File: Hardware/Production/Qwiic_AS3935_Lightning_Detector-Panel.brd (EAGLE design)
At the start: 123.2 x 123.2 mm, 1075 parts, among them U1 AS3935, U10 AS3935, U11 AS3935, U12 AS3935, U13 AS3935, U14 AS3935, U15 AS3935, U16 AS3935, U2 AS3935, U3 AS3935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

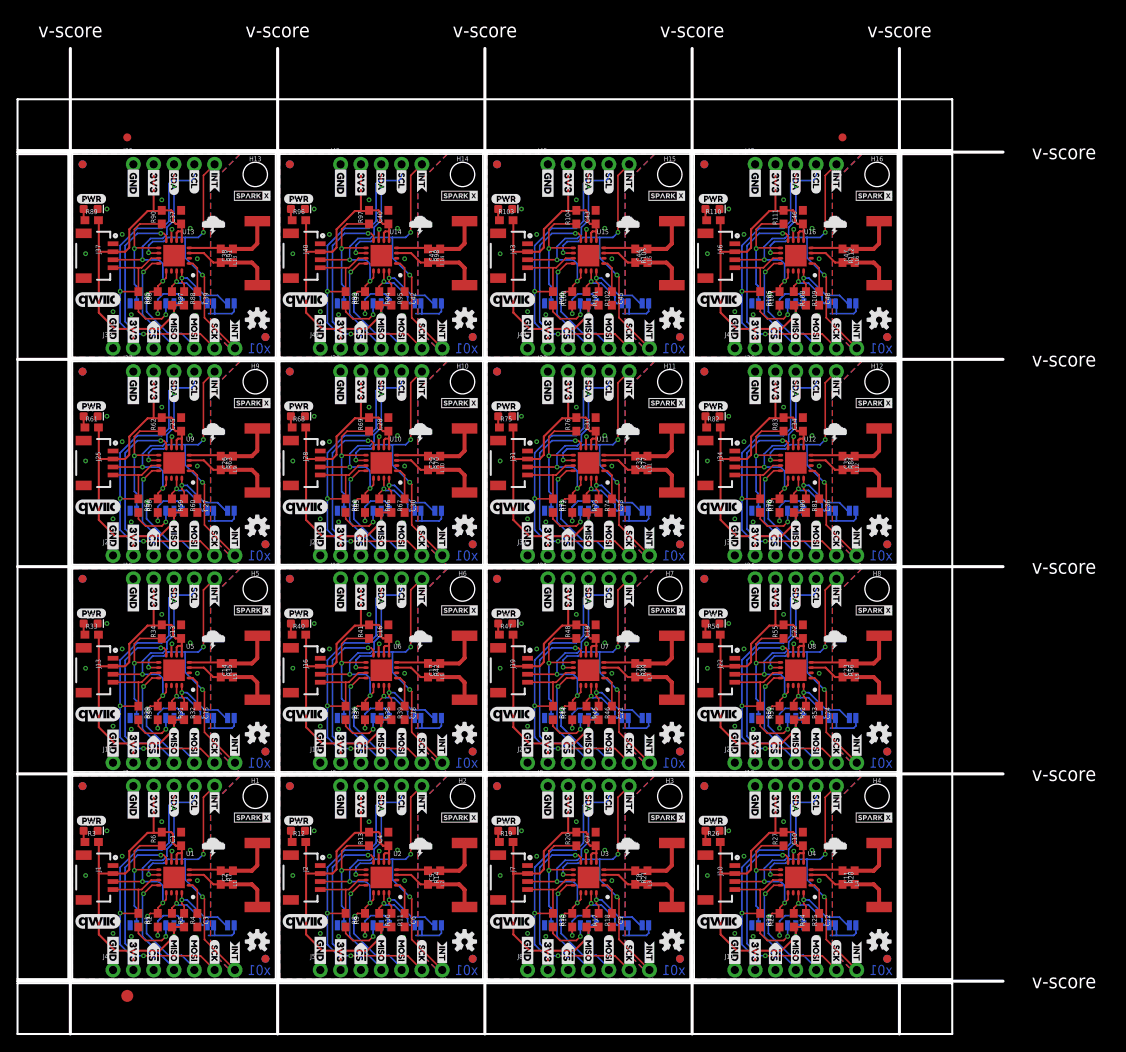
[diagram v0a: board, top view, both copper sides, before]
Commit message: Version x02 Exposed pad underneath was not connected to ground, coil package was incorrect.
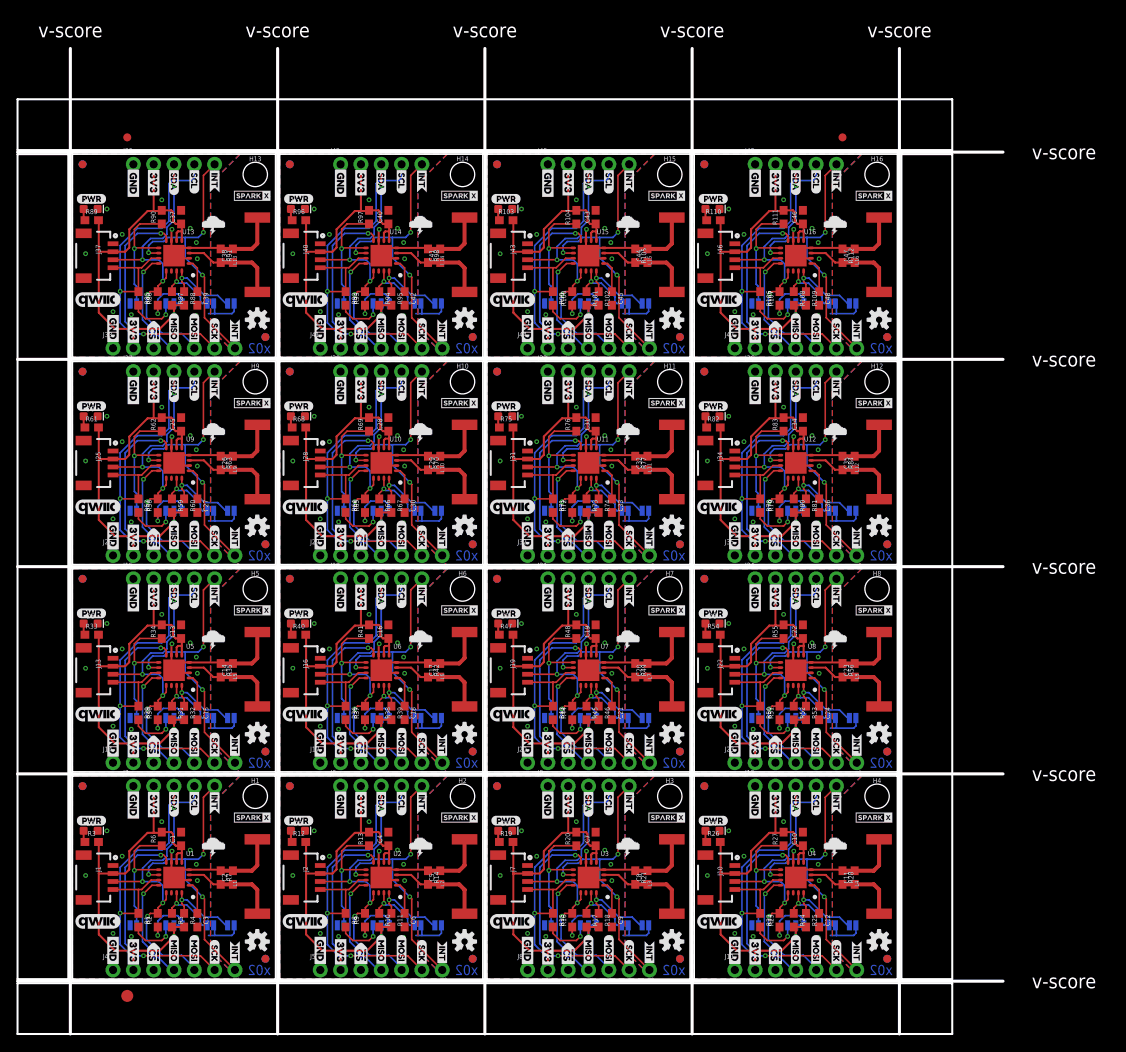
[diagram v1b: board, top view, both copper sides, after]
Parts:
- R105, R112, R14, R21, R28, R35, R42, R49, R56, R63, R7, R70, R77, R84, R91, R98: value 10 -> 10k
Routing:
- net GND11: track 18.7 -> 25.6 mm, vias 10 -> 11
- net GND10: track 18.7 -> 25.6 mm, vias 10 -> 11
- net GND3: track 18.7 -> 25.6 mm, vias 10 -> 11
- net GND2: track 18.7 -> 25.6 mm, vias 10 -> 11
- net GND9: track 18.7 -> 25.6 mm, vias 10 -> 11
- net GND7: track 18.7 -> 25.6 mm, vias 10 -> 11
- net GND6: track 18.7 -> 25.6 mm, vias 10 -> 11
- net GND15: track 18.7 -> 25.6 mm, vias 10 -> 11
- net GND14: track 18.7 -> 25.6 mm, vias 10 -> 11
- net GND8: track 18.7 -> 25.6 mm, vias 10 -> 11
- net GND1: track 18.7 -> 25.6 mm, vias 10 -> 11
- net GND: track 18.7 -> 25.6 mm, vias 10 -> 11
- net GND5: track 18.7 -> 25.6 mm, vias 10 -> 11
- net GND4: track 18.7 -> 25.6 mm, vias 10 -> 11
- net GND13: track 18.7 -> 25.6 mm, vias 10 -> 11
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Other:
- board text added: "x02"
- board text removed: "x01"

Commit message: One more time
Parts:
- removed FRAME1, FRAME10, FRAME11, FRAME12, FRAME13, FRAME14, FRAME15, FRAME16, FRAME2, FRAME3, FRAME4, FRAME5, FRAME6, FRAME7, FRAME8, FRAME9: FRAME-LETTER, SparkFun-Aesthetics:CREATIVE_COMMONS
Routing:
- net GND7: track 25.6 -> 22.7 mm
- net GND6: track 25.6 -> 22.7 mm
- net GND5: track 25.6 -> 22.7 mm
- net GND4: track 25.6 -> 22.7 mm
- net GND3: track 25.6 -> 22.7 mm
- net GND2: track 25.6 -> 22.7 mm
- net GND1: track 25.6 -> 22.7 mm
- net GND: track 25.6 -> 22.7 mm
- net GND9: track 25.6 -> 22.7 mm
- net GND15: track 25.6 -> 22.7 mm
- net GND14: track 25.6 -> 22.7 mm
- net GND13: track 25.6 -> 22.7 mm
- net GND11: track 25.6 -> 22.7 mm
- net GND10: track 25.6 -> 22.7 mm
- net GND8: track 25.6 -> 22.7 mm
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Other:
- board text removed: "Elias Santistevan"
